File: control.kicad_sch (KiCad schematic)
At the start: 13 parts, among them J1 Wurth_THR_Terminal_M4, J2 Wurth_THR_Terminal_M4, J3 Wurth_THR_Terminal_M4, J4 Conn_01x03, J5 Conn_02x20_Odd_Even, J6 TE_Faston_20-16AWG_Straight_T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, J7 TE_Faston_20-16AWG_Straight_T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, U1 TPS7B8733, U2 MAX33071

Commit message: add header footprints
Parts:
- J4: footprint (none) -> Connector_PinHeader_2.54mm:PinHeader_1x03_P2.54mm_Vertical
- J5: footprint (none) -> Connector_PinHeader_2.54mm:PinHeader_2x20_P2.54mm_Vertical
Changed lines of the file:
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@@
     (property "Reference" "J5" (id 0) (at 228.6 92.71 0))
     (property "Value" "Conn_02x20_Odd_Even" (id 1) (at 228.6 95.25 0))
-    (property "Footprint" "" (id 2) (at 227.33 121.92 0)
+    (property "Footprint" "Connector_PinHeader_2.54mm:PinHeader_2x20_P2.54mm_Vertical" (id 2) (at 227.33 121.92 0)
       (effects (font (size 1.27 1.27)) hide)
     )
@@
       (effects (font (size 1.27 1.27)) (justify left))
     )
-    (property "Footprint" "" (id 2) (at 153.67 162.56 0)
+    (property "Footprint" "Connector_PinHeader_2.54mm:PinHeader_1x03_P2.54mm_Vertical" (id 2) (at 153.67 162.56 0)
       (effects (font (size 1.27 1.27)) hide)
     )
@@
     )
     (path "/69e54dfb-ac9d-4c46-a779-f903052ebcce"
-      (reference "J4") (unit 1) (value "Conn_01x03") (footprint "")
+      (reference "J4") (unit 1) (value "Conn_01x03") (footprint "Connector_PinHeader_2.54mm:PinHeader_1x03_P2.54mm_Vertical")
     )
     (path "/44b2219f-f1ac-470a-a0c7-0dafc1b7cc1e"
-      (reference "J5") (unit 1) (value "Conn_02x20_Odd_Even") (footprint "")
+      (reference "J5") (unit 1) (value "Conn_02x20_Odd_Even") (footprint "Connector_PinHeader_2.54mm:PinHeader_2x20_P2.54mm_Vertical")
     )
     (path "/67db03dc-cb2f-47ff-b566-a38be36b10a9"

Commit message: add basic TVS
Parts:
- added D? (x2): SZ1.5SMC36AT3G, symbol Device:D_Zener
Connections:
- net +12C: now also D?.1 (K)
- net +12V: now also D?.1 (K)
- net GNDREF: now also D?.2 (A), D?.2 (A)
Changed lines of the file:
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@@
 (kicad_sch (version 20211123) (generator eeschema)
   (paper "A4")
+  (junction (at 137.16 45.72) (diameter 0) (color 0 0 0 0)
+  )
   (junction (at 220.98 34.29) (diameter 0) (color 0 0 0 0)
   )
@@
     (stroke (width 0) (type default) (color 0 0 0 0))
   )
+  (wire (pts (xy 142.24 45.72) (xy 142.24 41.91))
+    (stroke (width 0) (type default) (color 0 0 0 0))
+  )
   (wire (pts (xy 219.71 46.99) (xy 222.25 46.99))
     (stroke (width 0) (type default) (color 0 0 0 0))
@@
     (stroke (width 0) (type default) (color 0 0 0 0))
   )
+  (wire (pts (xy 142.24 31.75) (xy 142.24 34.29))
+    (stroke (width 0) (type default) (color 0 0 0 0))
+  )
   (wire (pts (xy 86.36 35.56) (xy 86.36 41.91))
     (stroke (width 0) (type default) (color 0 0 0 0))
@@
     (stroke (width 0) (type default) (color 0 0 0 0))
   )
+  (wire (pts (xy 132.08 31.75) (xy 132.08 34.29))
+    (stroke (width 0) (type default) (color 0 0 0 0))
+  )
   (wire (pts (xy 214.63 21.59) (xy 214.63 24.13))
     (stroke (width 0) (type default) (color 0 0 0 0))
@@
     (stroke (width 0) (type default) (color 0 0 0 0))
   )
+  (wire (pts (xy 137.16 45.72) (xy 137.16 46.99))
+    (stroke (width 0) (type default) (color 0 0 0 0))
+  )
   (bus (pts (xy 88.9 105.41) (xy 88.9 107.95))
     (stroke (width 0) (type default) (color 0 0 0 0))
@@
     (stroke (width 0) (type default) (color 0 0 0 0))
   )
+  (wire (pts (xy 132.08 41.91) (xy 132.08 45.72))
+    (stroke (width 0) (type default) (color 0 0 0 0))
+  )
   (bus (pts (xy 88.9 83.82) (xy 88.9 87.63))
     (stroke (width 0) (type default) (color 0 0 0 0))
@@
     (stroke (width 0) (type default) (color 0 0 0 0))
   )
+  (wire (pts (xy 132.08 45.72) (xy 137.16 45.72))
+    (stroke (width 0) (type default) (color 0 0 0 0))
+  )
   (wire (pts (xy 237.49 142.24) (xy 241.3 142.24))
     (stroke (width 0) (type default) (color 0 0 0 0))
@@
   )
   (bus (pts (xy 88.9 87.63) (xy 88.9 100.33))
+    (stroke (width 0) (type default) (color 0 0 0 0))
+  )
+  (wire (pts (xy 137.16 45.72) (xy 142.24 45.72))
     (stroke (width 0) (type default) (color 0 0 0 0))
   )
@@
     (pin "1")
   )
+  (symbol (lib_id "Device:D_Zener") (at 132.08 38.1 270) (unit 1)
+    (in_bom yes) (on_board yes)
+    (property "Reference" "D?" (id 0) (at 127 36.83 90)
+      (effects (font (size 1.27 1.27)) (justify left))
+    )
+    (property "Value" "SZ1.5SMC36AT3G" (id 1) (at 113.03 39.37 90)
+      (effects (font (size 1.27 1.27)) (justify left))
+    )
+    (property "Footprint" "" (id 2) (at 132.08 38.1 0)
+      (effects (font (size 1.27 1.27)) hide)
+    )
+    (property "Datasheet" "~" (id 3) (at 132.08 38.1 0)
+      (effects (font (size 1.27 1.27)) hide)
+    )
+    (pin "1")
+    (pin "2")
+  )
+  (symbol (lib_id "power:GNDREF") (at 137.16 46.99 0) (unit 1)
+    (in_bom yes) (on_board yes) (fields_autoplaced)
+    (property "Reference" "#PWR?" (id 0) (at 137.16 53.34 0)
+      (effects (font (size 1.27 1.27)) hide)
+    )
+    (property "Value" "GNDREF" (id 1) (at 137.16 52.07 0))
+    (property "Footprint" "" (id 2) (at 137.16 46.99 0)
+      (effects (font (size 1.27 1.27)) hide)
+    )
+    (property "Datasheet" "" (id 3) (at 137.16 46.99 0)
+      (effects (font (size 1.27 1.27)) hide)
+    )
+    (pin "1")
+  )
   (symbol (lib_id "power:+12V") (at 215.9 147.32 90) (unit 1)
     (in_bom yes) (on_board yes) (fields_autoplaced)
@@
     (pin "1")
   )
+  (symbol (lib_id "power:+12C") (at 132.08 31.75 0) (unit 1)
+    (in_bom yes) (on_board yes) (fields_autoplaced)
+    (property "Reference" "#PWR?" (id 0) (at 132.08 35.56 0)
+      (effects (font (size 1.27 1.27)) hide)
+    )
+    (property "Value" "+12C" (id 1) (at 132.08 26.67 0))
+    (property "Footprint" "" (id 2) (at 132.08 31.75 0)
+      (effects (font (size 1.27 1.27)) hide)
+    )
+    (property "Datasheet" "" (id 3) (at 132.08 31.75 0)
+      (effects (font (size 1.27 1.27)) hide)
+    )
+    (pin "1")
+  )
   (symbol (lib_id "Toadly:Wurth_THR_Terminal_M4") (at 27.94 55.88 90) (unit 1)
     (in_bom yes) (on_board yes) (fields_autoplaced)
@@
     (pin "2")
   )
+  (symbol (lib_id "power:+12V") (at 142.24 31.75 0) (unit 1)
+    (in_bom yes) (on_board yes) (fields_autoplaced)
+    (property "Reference" "#PWR?" (id 0) (at 142.24 35.56 0)
+      (effects (font (size 1.27 1.27)) hide)
+    )
+    (property "Value" "+12V" (id 1) (at 142.24 26.67 0))
+    (property "Footprint" "" (id 2) (at 142.24 31.75 0)
+      (effects (font (size 1.27 1.27)) hide)
+    )
+    (property "Datasheet" "" (id 3) (at 142.24 31.75 0)
+      (effects (font (size 1.27 1.27)) hide)
+    )
+    (pin "1")
+  )
   (symbol (lib_id "power:GNDREF") (at 215.9 142.24 270) (unit 1)
     (in_bom yes) (on_board yes)
@@
     )
     (pin "1")
+  )
+  (symbol (lib_id "Device:D_Zener") (at 142.24 38.1 270) (unit 1)
+    (in_bom yes) (on_board yes)
+    (property "Reference" "D?" (id 0) (at 144.78 36.8299 90)
+      (effects (font (size 1.27 1.27)) (justify left))
+    )
+    (property "Value" "SZ1.5SMC36AT3G" (id 1) (at 144.78 39.3699 90)
+      (effects (font (size 1.27 1.27)) (justify left))
+    )
+    (property "Footprint" "" (id 2) (at 142.24 38.1 0)
+      (effects (font (size 1.27 1.27)) hide)
+    )
+    (property "Datasheet" "~" (id 3) (at 142.24 38.1 0)
+      (effects (font (size 1.27 1.27)) hide)
+    )
+    (pin "1")
+    (pin "2")
   )
   (symbol (lib_id "Toadly:Wurth_THR_Terminal_M4") (at 27.94 26.67 90) (unit 1)
@@
       (reference "#PWR076") (unit 1) (value "GNDREF") (footprint "")
     )
+    (path "/5d406c89-8e06-4c75-9288-26d5442a50e2"
+      (reference "#PWR?") (unit 1) (value "GNDREF") (footprint "")
+    )
+    (path "/9948560a-0dd9-4297-82d3-caefb708df60"
+      (reference "#PWR?") (unit 1) (value "+12C") (footprint "")
+    )
+    (path "/e5971226-52de-409f-8d56-021f8cfafb15"
+      (reference "#PWR?") (unit 1) (value "+12V") (footprint "")
+    )
     (path "/07551e16-8169-4161-b345-aacecb867638/46e29b69-2a0c-42ee-8f6d-326576f705f9"
       (reference "A1") (unit 1) (value "Arduino_Nano_v3.x") (footprint "Module:Arduino_Nano")
@@
       (reference "D1") (unit 1) (value "1N4148W") (footprint "Diode_SMD:D_SOD-123")
     )
+    (path "/57c40a70-b0e0-475d-9c6c-d4cba4b8f0a1"
+      (reference "D?") (unit 1) (value "SZ1.5SMC36AT3G") (footprint "")
+    )
+    (path "/f36f72f8-5a4e-48b3-b45d-5dd9f3fd45df"
+      (reference "D?") (unit 1) (value "SZ1.5SMC36AT3G") (footprint "")
+    )
     (path "/f53f1c45-46e1-45cf-9db1-aa99e47f0316"

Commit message: many changes, update to KiCAD 7
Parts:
- D2, D3: renamed from D?; value SZ1.5SMC36AT3G -> D15V0HA1U2LP-7B; footprint (none) -> Diode_SMD:D_0402_1005Metric_Pad0.77x0.64mm_HandSolder

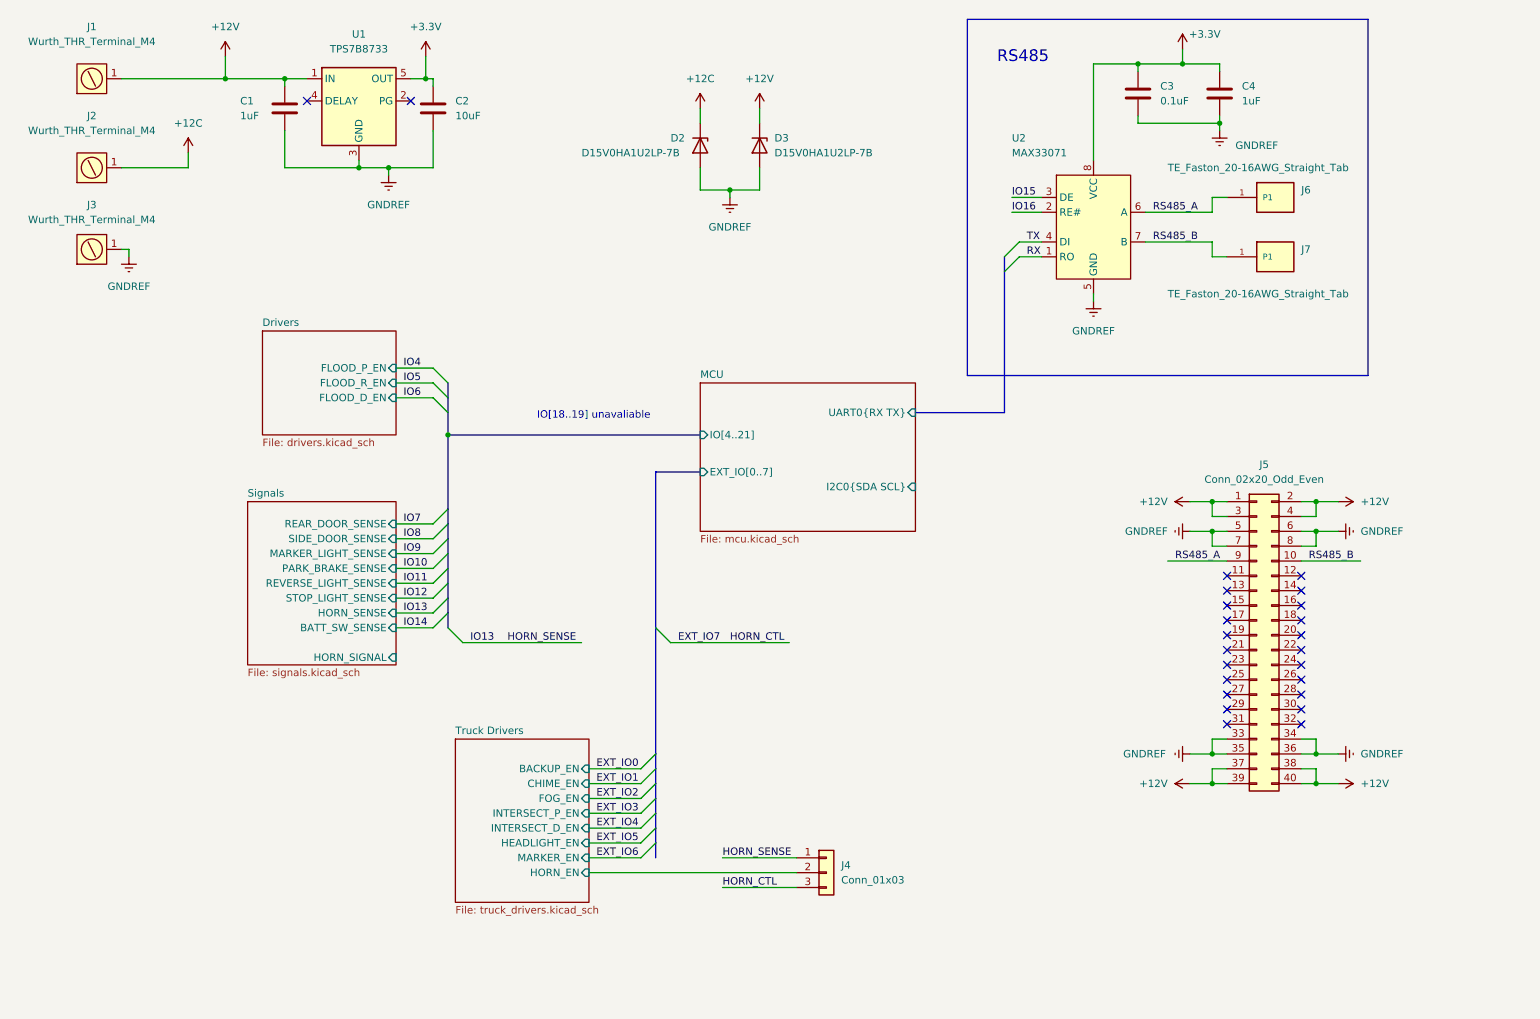
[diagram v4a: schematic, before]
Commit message: add compartment lights, switch to samd21j
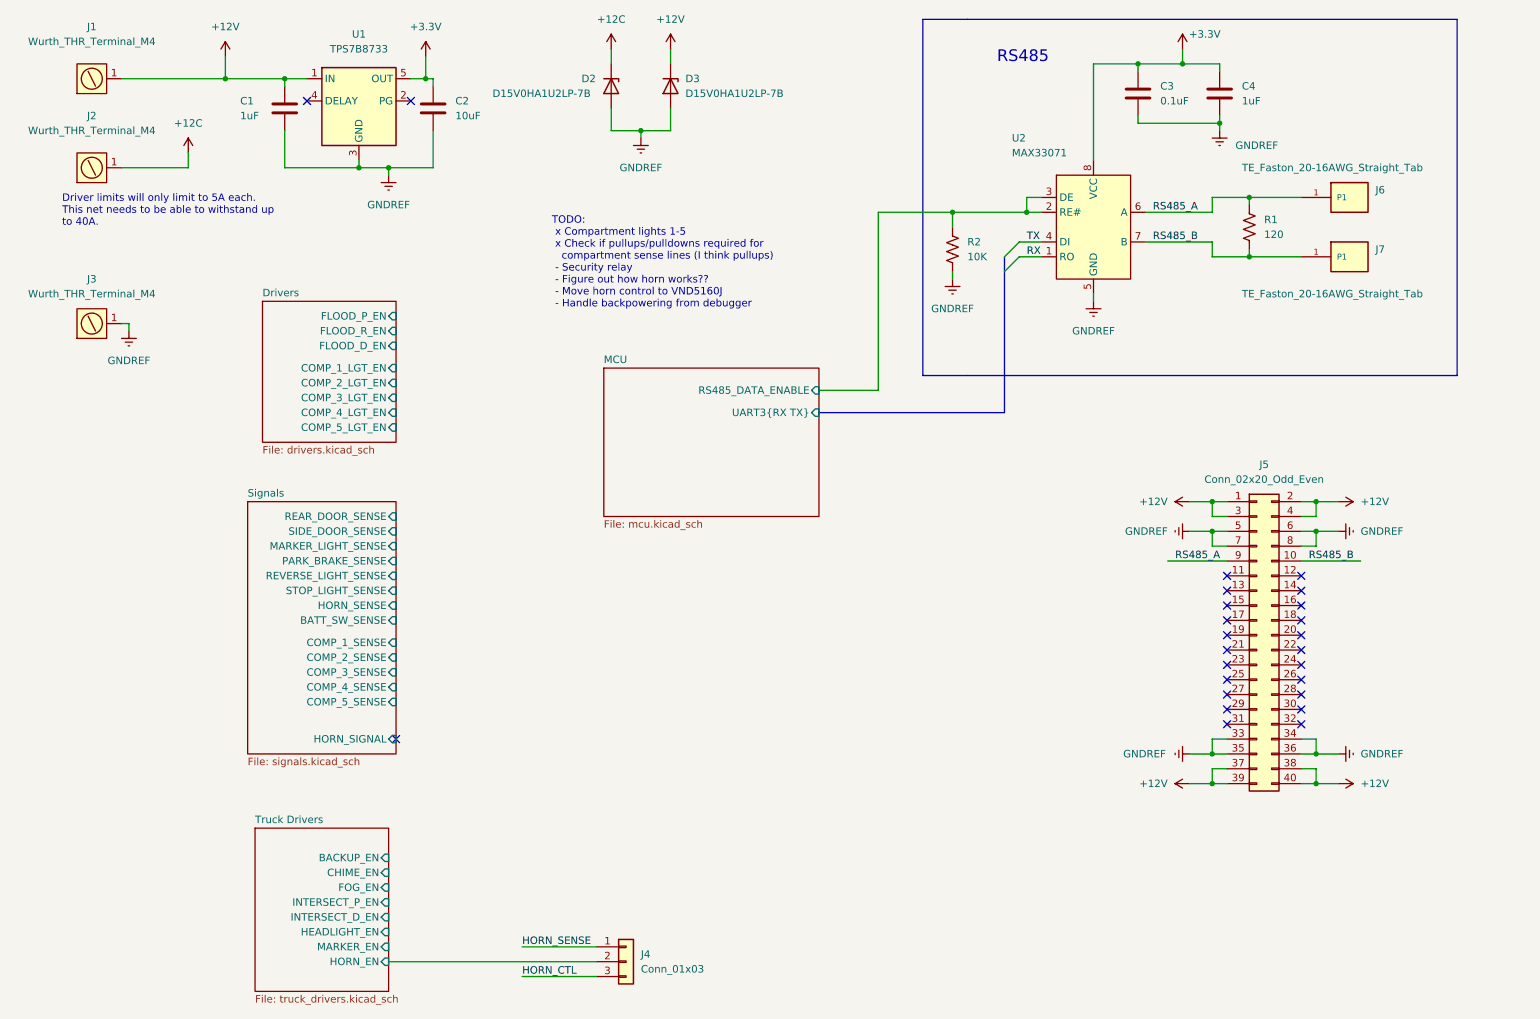
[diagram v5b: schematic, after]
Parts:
- added R1: 120, Resistor_SMD:R_0805_2012Metric_Pad1.20x1.40mm_HandSolder, symbol Device:R_US
- added R2: 10K, Resistor_SMD:R_0805_2012Metric_Pad1.20x1.40mm_HandSolder, symbol Device:R_US
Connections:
- net IO16 is gone; now on net MCU/RS485_DATA_ENABLE: U2.2 (RE#)
- net GNDREF: now also R2.2
- net RS485_A: now also R1.1
- net RS485_B: now also R1.2
- net EXT_IO7 renamed HORN_CTL
- net IO15 renamed MCU/RS485_DATA_ENABLE
- net MCU/RS485_DATA_ENABLE: now also R2.1
- no-connect marks 24 -> 25
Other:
- sheet Drivers ports: added COMP_1_LGT_EN, COMP_2_LGT_EN, COMP_3_LGT_EN, COMP_4_LGT_EN, COMP_5_LGT_EN; removed none
- sheet MCU ports: added RS485_DATA_ENABLE, UART3{RX TX}; removed EXT_IO[0..7], I2C0{SDA SCL}, IO[4..21], UART0{RX TX}
- sheet Signals ports: added COMP_1_SENSE, COMP_2_SENSE, COMP_3_SENSE, COMP_4_SENSE, COMP_5_SENSE; removed none
- note added: "Driver limits will only limit to 5A each. This net needs to be able to withstand up to 40A."
- note added: "TODO: x Compartment lights 1-5 x Check if pullups/pulldowns required for compartment sense lines (I think pullups) - Security relay - Figure out how horn works?? - Move horn control to VND5160J - Handle backpowering from debugger"
- note removed: "IO[18..19] unavaliable"
- moved on the sheet: D2, D3, J3, J4, J6, J7

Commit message: remove drivers
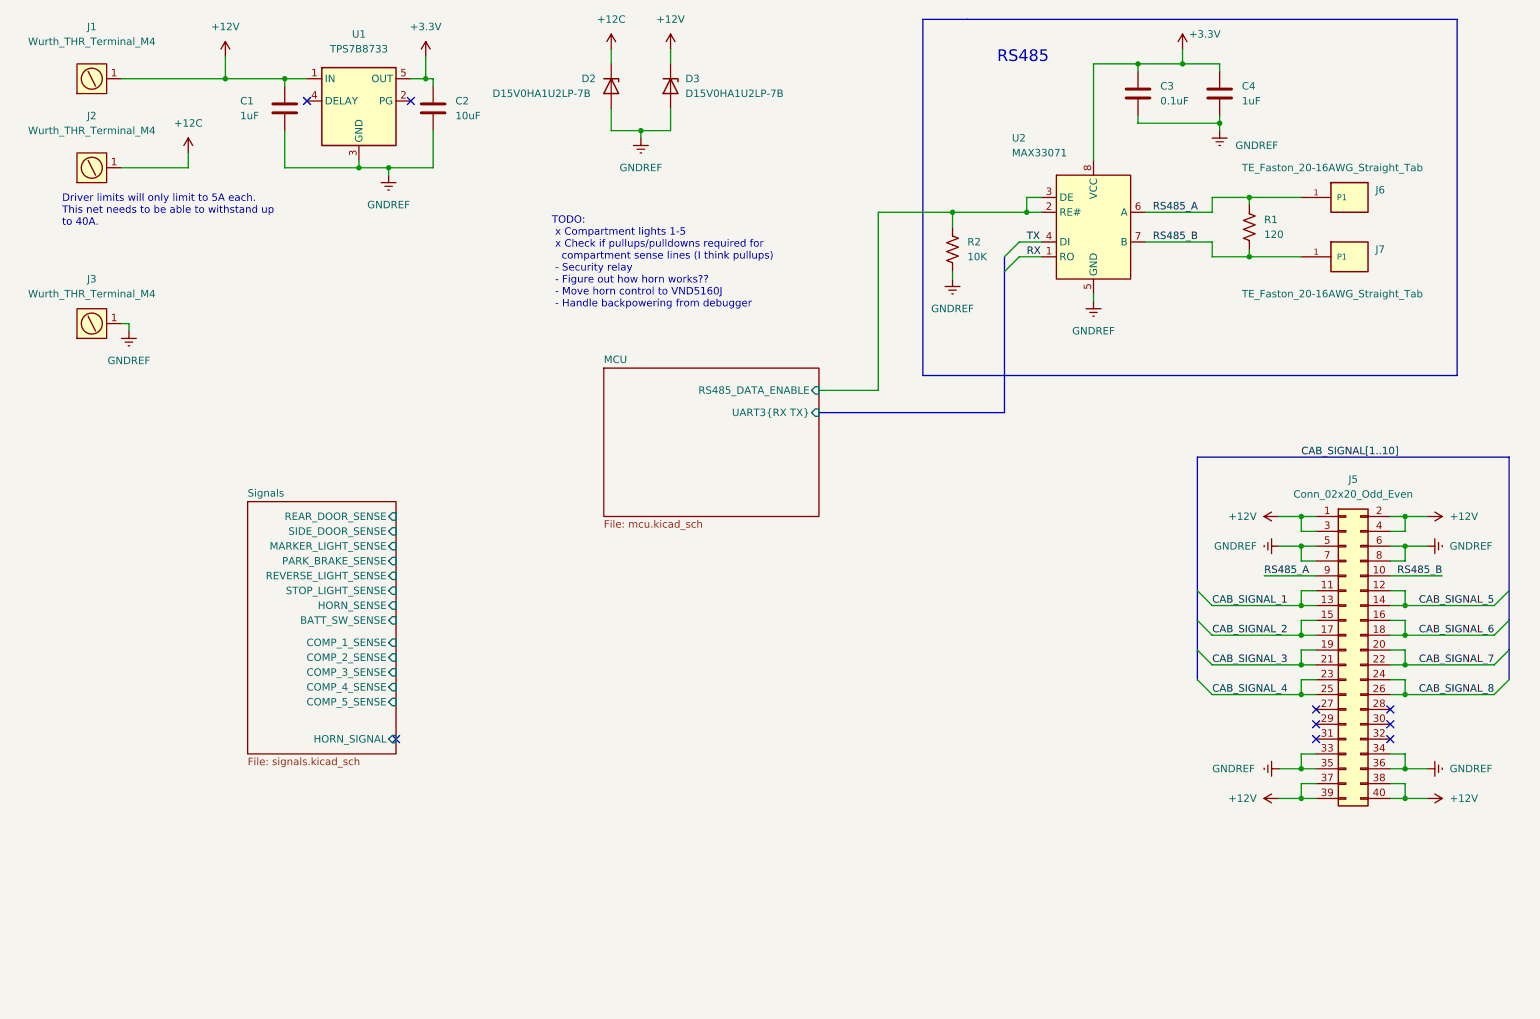
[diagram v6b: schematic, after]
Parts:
- removed J4: Conn_01x03, Connector_PinHeader_2.54mm:PinHeader_1x03_P2.54mm_Vertical, symbol Connector_Generic:Conn_01x03
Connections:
- net CAB_SIGNAL_1: now reaches J5.11 (Pin_11)
- net CAB_SIGNAL_1: now also J5.13 (Pin_13)
- net CAB_SIGNAL_5: now reaches J5.12 (Pin_12)
- net CAB_SIGNAL_5: now also J5.14 (Pin_14)
- net CAB_SIGNAL_2: now reaches J5.15 (Pin_15)
- net CAB_SIGNAL_2: now also J5.17 (Pin_17)
- net CAB_SIGNAL_6: now reaches J5.16 (Pin_16)
- net CAB_SIGNAL_6: now also J5.18 (Pin_18)
- net CAB_SIGNAL_3: now reaches J5.19 (Pin_19)
- net CAB_SIGNAL_3: now also J5.21 (Pin_21)
- net CAB_SIGNAL_7: now reaches J5.20 (Pin_20)
- net CAB_SIGNAL_7: now also J5.22 (Pin_22)
- net CAB_SIGNAL_4: now reaches J5.23 (Pin_23)
- net CAB_SIGNAL_4: now also J5.25 (Pin_25)
- net CAB_SIGNAL_8: now reaches J5.24 (Pin_24)
- net CAB_SIGNAL_8: now also J5.26 (Pin_26)
- no-connect marks 25 -> 9
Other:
- removed sheet Drivers
- removed sheet Truck Drivers
- moved on the sheet: J5
